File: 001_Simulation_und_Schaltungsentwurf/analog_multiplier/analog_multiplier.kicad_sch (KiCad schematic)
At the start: 11 parts, among them IC1 MPY634KP, IC2 MPY634KP

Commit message: Weiterarbeit an Sim Plots
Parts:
- added C3: {c}, symbol Device:C_Small
- added IC3, IC4: MPY634KP, DIP794W53P254L1930H508Q14N, symbol BA_Footprints:MPY634KP
- added U1, U2: TL082, Package_DIP:CERDIP-8_W7.62mm_SideBrazed_LongPads_Socket, symbol Amplifier_Operational:TL082
- added V3, V4: VSIN, symbol Simulation_SPICE:VSIN
- added V5: VPWL, symbol Simulation_SPICE:VPWL
- added V6: 5, symbol Simulation_SPICE:VDC
- added V9: 10, symbol Simulation_SPICE:VDC
- C1, C2: value 0.1u -> {c}
- R1, R3: value 1k -> {R}; footprint (none) -> 000_Footprints:Resistor
- R2: value {Rx} -> {R}; footprint (none) -> 000_Footprints:Resistor
- V7: renamed from V4; value 10 -> 15
- V8: renamed from V5; value 10 -> 15
- renumbered V3 to V1, V1 to V2
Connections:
- net +10V: now also IC3.4 (SCALE_FACTOR), IC4.4 (SCALE_FACTOR), V9.1; no longer IC1.14 (+VS), IC2.14 (+VS), V8.1
- net GND: now also IC3.10 (Z_2_INPUT), IC3.2 (X_2_INPUT), IC3.7 (Y_2_INPUT), IC4.10 (Z_2_INPUT), IC4.2 (X_2_INPUT), IC4.7 (Y_2_INPUT), U1.3 (+), U1.5 (+), U2.3 (+), V3.2, V4.2, V5.2, V6.2, V9.2; no longer C2.2, R2.1
- net mult1_y: now also IC3.6 (Y_1_INPUT)
- net at R2.2: now also C2.1, U1.6 (-); no longer C1.2
- net mult_out_0: now reaches IC2.11 (Z_1_INPUT), IC2.12 (OUTPUT)
- net mult_out_0: now also R2.1; no longer R3.1
- net mult_out_90: now reaches IC1.11 (Z_1_INPUT), IC1.12 (OUTPUT), R1.1
- net -10V renamed -15V
- net -15V: now also IC3.8 (-VS), IC4.8 (-VS), U1.4 (V-), U2.4 (V-)
- net mult1_out: no longer names the net of C1.1, R1.2
- net mult1_out: now also U1.2 (-)
- net mult1_x renamed in_90
- net in_90: no longer IC2.1 (X_1_INPUT)
- net mult2_out: no longer names the net of R3.2
- net mult2_out: now also C3.1, U2.2 (-); no longer C2.1
- new net +15V: IC1.14 (+VS), IC2.14 (+VS), IC3.14 (+VS), IC4.14 (+VS), U1.8 (V+), U2.8 (V+), V8.1
- new net detec_out0: C2.2, U1.7
- new net detec_out180: C3.2, U2.1
- new net detec_out90: C1.2, U1.1
- new net in1_dc: IC4.1 (X_1_INPUT), V5.1
- new net in2_dc: IC4.6 (Y_1_INPUT), V6.1
- new net in_0: IC2.1 (X_1_INPUT), V3.1
- new net in_180: IC3.1 (X_1_INPUT), V4.1
- new net mult_out_180: IC3.11 (Z_1_INPUT), IC3.12 (OUTPUT), R3.1
- new net out_dc: IC4.11 (Z_1_INPUT), IC4.12 (OUTPUT)
- no-connect marks 8 -> 16
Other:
- note added: ".control set controlswait write analog_multiplier.raw all .endc"
- note added: ".param phi180 = 180 .param phi90 = 90 .param phi0 = 0 .param R = 1k .param c = 1u"
- note removed: ".param phi = 90"
- moved on the sheet: IC1, IC2, V1, V2, V7, V8

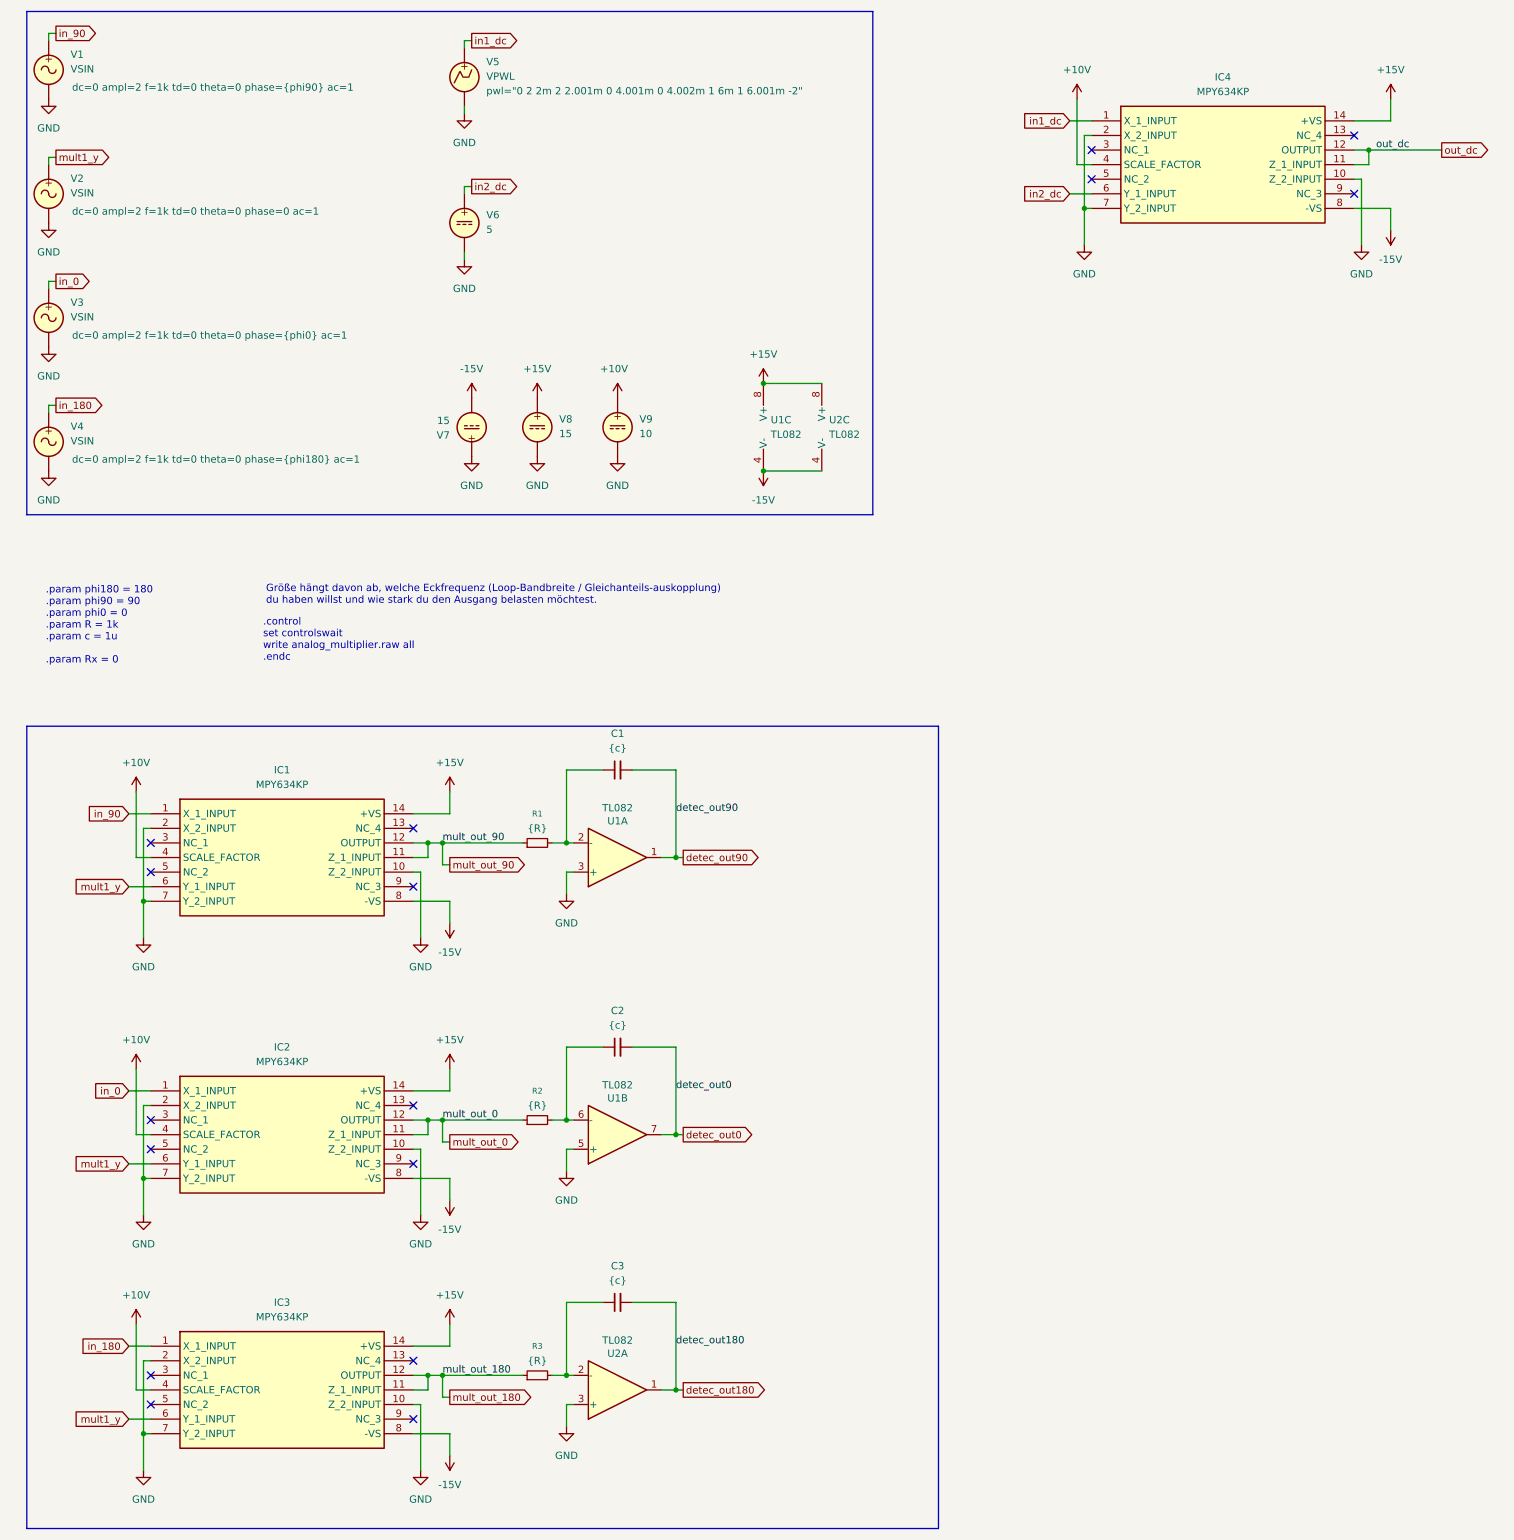
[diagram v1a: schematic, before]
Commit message: Überarbeitung von SP und Plots
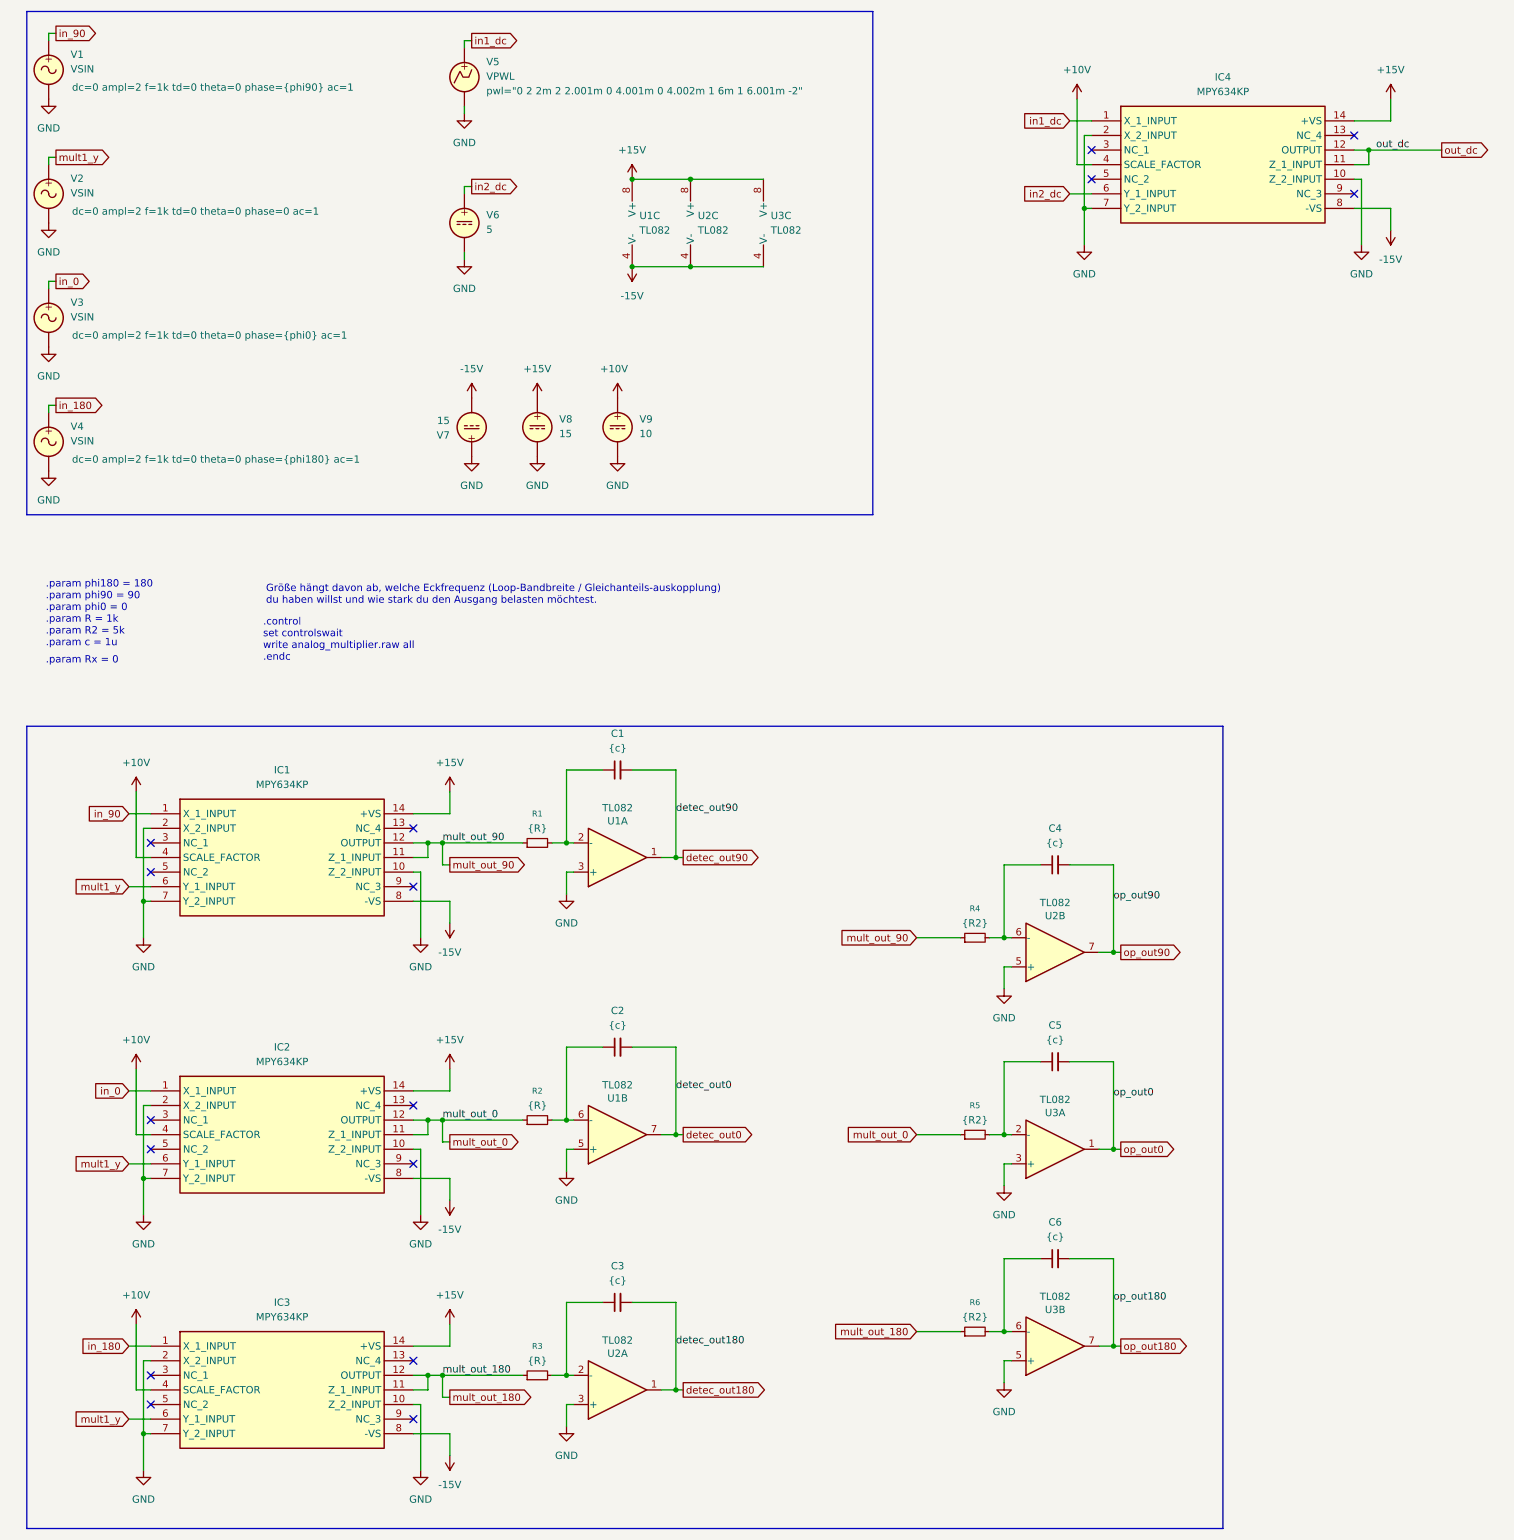
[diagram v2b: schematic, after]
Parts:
- added C4, C5, C6: {c}, symbol Device:C_Small
- added R4, R5, R6: {R2}, 000_Footprints:Resistor, symbol Device:R_Small
- added unit 2 of U2
- added U3: TL082, Package_DIP:CERDIP-8_W7.62mm_SideBrazed_LongPads_Socket, symbol Amplifier_Operational:TL082
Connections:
- net +15V: now also U3.8 (V+)
- net -15V: now also U3.4 (V-)
- net GND: now also U2.5 (+), U3.3 (+), U3.5 (+)
- net mult_out_0: now also R5.1
- net mult_out_180: now also R6.1
- net mult_out_90: now also R4.1
- new net: C6.1, R6.2, U3.6 (-)
- new net: C4.1, R4.2, U2.6 (-)
- new net: C5.1, R5.2, U3.2 (-)
- new net op_out0: C5.2, U3.1
- new net op_out180: C6.2, U3.7
- new net op_out90: C4.2, U2.7
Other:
- note added: ".param phi180 = 180 .param phi90 = 90 .param phi0 = 0 .param R = 1k .param R2 = 5k .param c = 1u"
- note removed: ".param phi180 = 180 .param phi90 = 90 .param phi0 = 0 .param R = 1k .param c = 1u"
- moved on the sheet: U1C, U2C
